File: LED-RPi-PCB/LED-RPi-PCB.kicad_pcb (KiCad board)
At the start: 2 copper layers, 58.8 x 44.1 mm, 27 parts, among them J1 FAN_CON, J2 RPi_IN, J3 GND_CON, J4 12V_CON, J5 5V_CON, J6 3V3_CON, J7 Jack-DC, J8 GND_CON, Q1 2N2222A, U1 MP2307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

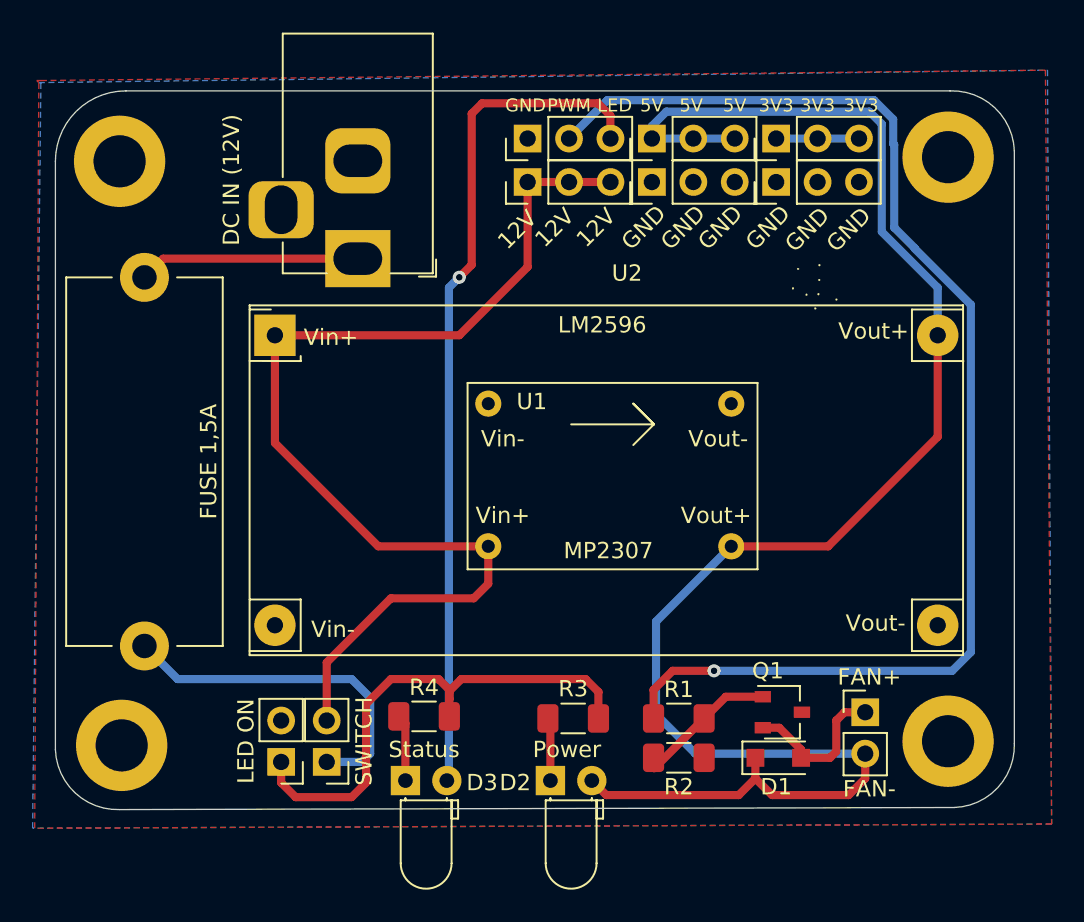
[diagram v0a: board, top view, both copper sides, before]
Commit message: Creada PCB para controlar motores con PWM y Transistor. Añadidos logos DCD
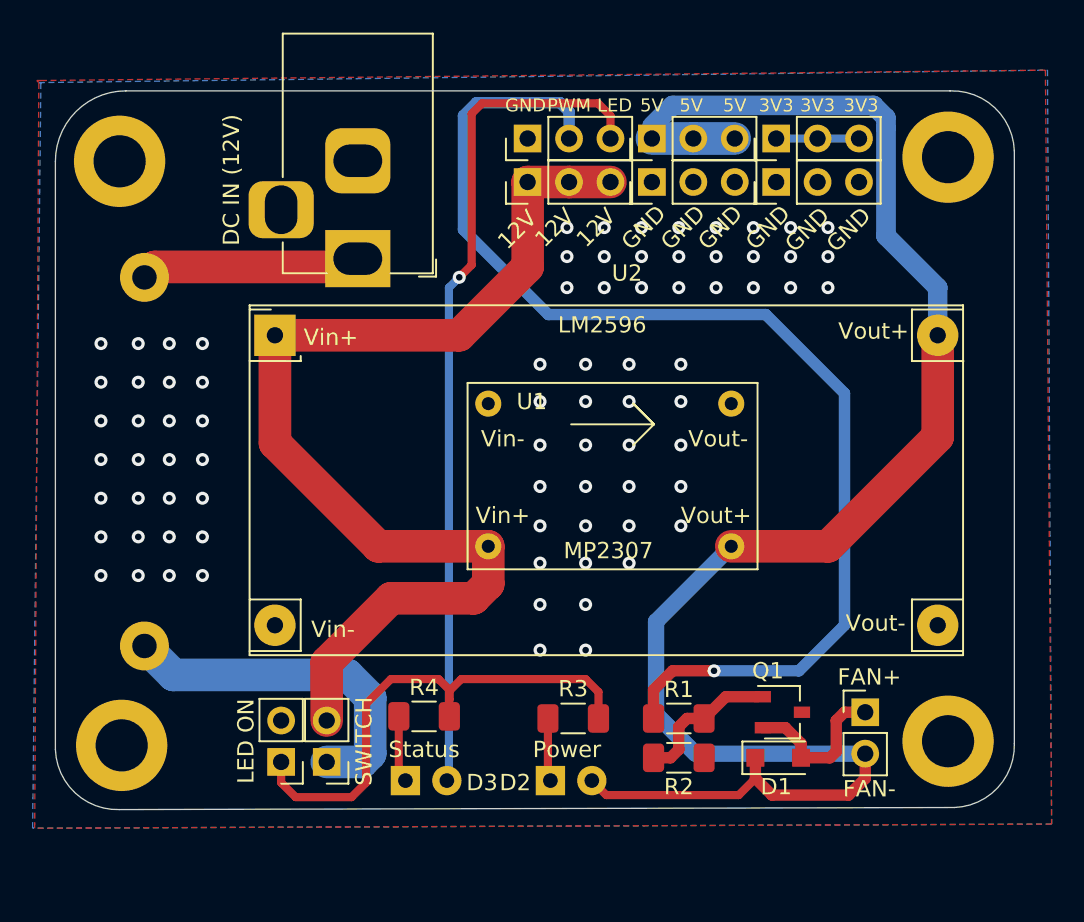
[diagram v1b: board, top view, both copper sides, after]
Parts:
- removed the G*** at (122.6, 95.1)
- removed REF**: KiCad-Logo2_5mm_SilkScreen, Symbol:KiCad-Logo2_5mm_SilkScreen
- added G***: LOGO, logo:Logo_DC, B.Cu at (109.7, 107.4)
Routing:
- net PWM: track 78.1 -> 72.5 mm
- net VDC: track 13.6 -> 15.2 mm
- net +5V: track 104.0 -> 104.7 mm
- net Net-(Q1-Pad1): track 8.36 -> 8.91 mm
- net GND: vias 0 -> 79
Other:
- net class Default removed
- board text added: "digitalcodesign.com"
- board text removed: "FUSE 1,5A"

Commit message: Añadidos las README así como GERBERS y RENDERs
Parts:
- removed G***: LOGO, logo:Logo_DC
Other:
- board text removed: "digitalcodesign.com"
